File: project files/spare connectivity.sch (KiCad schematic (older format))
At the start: 1 part, among them J3 Target STDC-14

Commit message: some rerouting
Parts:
- added U3: STM32F103CBUx, Package_DFN_QFN:QFN-48-1EP_7x7mm_P0.5mm_EP5.6x5.6mm, symbol MCU_ST_STM32F1:STM32F103CBUx
- renumbered J3 to J6
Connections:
- net GNDD: now also U3.23 (VSS), U3.35 (VSS), U3.47 (VSS), U3.49 (VSS), U3.8 (VSSA)
- new net +3V3: U3.1 (VBAT), U3.24 (VDD), U3.36 (VDD), U3.48 (VDD), U3.9 (VDDA)
- new net AIN: U3.10 (PA0)
- new net BOOT_0: U3.44 (BOOT0)
- new net BOOT_1: U3.20 (PB2)
- new net Board_ID: U3.2 (PC13)
- new net OSC_IN: U3.5 (PD0)
- new net OSC_OUT: U3.6 (PD1)
- new net SELF_NRST: U3.7 (NRST)
- new net STLINK_LED: U3.30 (PA9)
- new net STLINK_RX: U3.13 (PA3)
- new net STLINK_TX: U3.12 (PA2)
- new net STLINK_USB_D+: U3.33 (PA12)
- new net STLINK_USB_D-: U3.32 (PA11)
- new net SWDCLK: U3.37 (PA14)
- new net SWDIO: U3.34 (PA13)
- new net SWO: U3.39 (PB3)
- new net T_JTDI: U3.17 (PA7)
- new net T_NRST_SWD: U3.18 (PB0)
- new net T_NRST_SWIM: U3.42 (PB6)
- new net T_NRST_SWIM_IN: U3.41 (PB5)
- new net T_SWDCLK: U3.15 (PA5), U3.26 (PB13)
- new net T_SWDIO: U3.27 (PB14)
- new net T_SWDIO_IN: U3.25 (PB12)
- new net T_SWIM: U3.22 (PB11), U3.45 (PB8)
- new net T_SWIM_IN: U3.21 (PB10), U3.43 (PB7), U3.46 (PB9)
- new net T_SWO: U3.31 (PA10)
- new net USB_RENUMn: U3.38 (PA15)
- no-connect marks 1 -> 10
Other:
- note added: "Second microcontroller is added for possibility to use different package.\nSolder one microcontroller only."
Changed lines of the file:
@@
 P 2950 3400
 AR Path="/5EC35CB1" Ref="#PWR?"  Part="1"
-AR Path="/5EC31CA9/5EC35CB1" Ref="#PWR0103"  Part="1"
-F 0 "#PWR0103" H 2950 3150 50  0001 C CNN
+AR Path="/5EC31CA9/5EC35CB1" Ref="#PWR050"  Part="1"
+F 0 "#PWR050" H 2950 3150 50  0001 C CNN
 F 1 "GNDD" H 2954 3245 50  0000 C CNN
 F 2 "" H 2950 3400 50  0001 C CNN
@@
 P 3200 3400
 AR Path="/5EC35CBA" Ref="#PWR?"  Part="1"
-AR Path="/5EC31CA9/5EC35CBA" Ref="#PWR0104"  Part="1"
-F 0 "#PWR0104" H 3200 3150 50  0001 C CNN
+AR Path="/5EC31CA9/5EC35CBA" Ref="#PWR051"  Part="1"
+F 0 "#PWR051" H 3200 3150 50  0001 C CNN
 F 1 "GNDD" H 3204 3245 50  0000 C CNN
 F 2 "" H 3200 3400 50  0001 C CNN
@@
 P 2950 2650
 AR Path="/5EC35CC7" Ref="J?"  Part="1"
-AR Path="/5EC31CA9/5EC35CC7" Ref="J3"  Part="1"
-F 0 "J3" H 2507 2696 50  0000 R CNN
+AR Path="/5EC31CA9/5EC35CC7" Ref="J6"  Part="1"
+F 0 "J6" H 2507 2696 50  0000 R CNN
 F 1 "Target STDC-14" H 2507 2605 50  0000 R CNN
 F 2 "Connector_PinHeader_1.27mm:PinHeader_2x07_P1.27mm_Vertical_SMD" H 2950 2650 50  0001 C CNN
@@
 Text GLabel 2900 1900 0    50   Input ~ 0
 T_Vref
+Wire Wire Line
+	9750 6100 9750 6050
+Wire Wire Line
+	9650 6050 9650 6100
+Connection ~ 9650 6100
+Wire Wire Line
+	9650 6100 9750 6100
+Wire Wire Line
+	9550 6050 9550 6100
+Connection ~ 9550 6100
+Wire Wire Line
+	9550 6100 9650 6100
+Wire Wire Line
+	9450 6050 9450 6100
+Connection ~ 9450 6100
+Wire Wire Line
+	9450 6100 9550 6100
+Wire Wire Line
+	9350 6050 9350 6100
+Wire Wire Line
+	9350 6100 9450 6100
+$Comp
+L power:GNDD #PWR053
+U 1 1 5EC6BDFB
+P 9750 6150
+F 0 "#PWR053" H 9750 5900 50  0001 C CNN
+F 1 "GNDD" H 9754 5995 50  0000 C CNN
+F 2 "" H 9750 6150 50  0001 C CNN
+F 3 "" H 9750 6150 50  0001 C CNN
+	1    9750 6150
+	1    0    0    -1
+$EndComp
+Wire Wire Line
+	9750 6150 9750 6100
+Connection ~ 9750 6100
+Text Notes 6700 6300 0    50   Italic 10
+Second microcontroller is added for possibility to use different package.\nSolder one microcontroller only.
+NoConn ~ 10150 5150
+NoConn ~ 10150 4950
+NoConn ~ 10150 4750
+NoConn ~ 10150 4450
+NoConn ~ 8850 5850
+NoConn ~ 8850 4750
+NoConn ~ 8850 4450
+NoConn ~ 8850 4150
+NoConn ~ 8850 4050
+Wire Wire Line
+	9350 3050 9350 3000
+Wire Wire Line
+	9450 3050 9450 3000
+Wire Wire Line
+	9550 3050 9550 3000
+Wire Wire Line
+	9650 3050 9650 3000
+Wire Wire Line
+	9750 3050 9750 3000
+$Comp
+L MCU_ST_STM32F1:STM32F103CBUx U3
+U 1 1 5EC6BE12
+P 9550 4550
+F 0 "U3" H 9850 3000 50  0000 C CNN
+F 1 "STM32F103CBUx" H 10100 3100 50  0000 C CNN
+F 2 "Package_DFN_QFN:QFN-48-1EP_7x7mm_P0.5mm_EP5.6x5.6mm" H 8950 3150 50  0001 R CNN
+F 3 "http://www.st.com/st-web-ui/static/active/en/resource/technical/document/datasheet/CD00161566.pdf" H 9550 4550 50  0001 C CNN
+	1    9550 4550
+	1    0    0    -1
+$EndComp
+Text GLabel 10150 5250 2    50   BiDi ~ 0
+STLINK_LED
+Text GLabel 8850 3650 0    50   Input ~ 0
+OSC_IN
+Text GLabel 8850 3750 0    50   Input ~ 0
+OSC_OUT
+Text GLabel 8850 3450 0    50   Input ~ 0
+BOOT_0
+Text GLabel 8850 3250 0    50   Input ~ 0
+SELF_NRST
+Text GLabel 8850 3950 0    50   Input ~ 0
+Board_ID
+Text GLabel 10150 4350 2    50   Input ~ 0
+AIN
+Text GLabel 10150 5450 2    50   Input ~ 0
+STLINK_USB_D-
+Text GLabel 10150 5550 2    50   Input ~ 0
+STLINK_USB_D+
+Text GLabel 10150 5350 2    50   Input ~ 0
+T_SWO
+Text GLabel 10150 5650 2    50   Input ~ 0
+SWDIO
+Text GLabel 10150 5750 2    50   Input ~ 0
+SWDCLK
+Text GLabel 10150 5850 2    50   Input ~ 0
+USB_RENUMn
+Text GLabel 8850 4650 0    50   Input ~ 0
+SWO
+Text GLabel 8850 4550 0    50   Input ~ 0
+BOOT_1
+Text GLabel 8850 5650 0    50   Input ~ 0
+T_SWDCLK
+Text GLabel 8850 4350 0    50   Input ~ 0
+T_NRST_SWD
+Text GLabel 8850 5350 0    50   Input ~ 0
+T_SWIM_IN
+Text GLabel 8850 5250 0    50   Input ~ 0
+T_SWIM_IN
+Text GLabel 8850 5050 0    50   Input ~ 0
+T_SWIM_IN
+Text GLabel 8850 4850 0    50   Input ~ 0
+T_NRST_SWIM_IN
+Text GLabel 8850 5750 0    50   Input ~ 0
+T_SWDIO
+Text GLabel 8850 4950 0    50   Input ~ 0
+T_NRST_SWIM
+Text GLabel 8850 5550 0    50   Input ~ 0
+T_SWDIO_IN
+Text GLabel 8850 5150 0    50   Input ~ 0
+T_SWIM
+Text GLabel 8850 5450 0    50   Input ~ 0
+T_SWIM
+Text GLabel 10150 4850 2    50   Input ~ 0
+T_SWDCLK
+Text GLabel 10150 4650 2    50   Output ~ 0
+STLINK_RX
+Text GLabel 10150 4550 2    50   Input ~ 0
+STLINK_TX
+Text GLabel 10150 5050 2    50   Input ~ 0
+T_JTDI
+Wire Wire Line
+	9350 3000 9450 3000
+Connection ~ 9450 3000
+Wire Wire Line
+	9450 3000 9550 3000
+Connection ~ 9550 3000
+Wire Wire Line
+	9550 3000 9650 3000
+Connection ~ 9650 3000
+Wire Wire Line
+	9650 3000 9750 3000
+$Comp
+L power:+3.3V #PWR052
+U 1 1 5EC6FD9F
+P 9550 3000
+F 0 "#PWR052" H 9550 2850 50  0001 C CNN
+F 1 "+3.3V" H 9565 3173 50  0000 C CNN
+F 2 "" H 9550 3000 50  0001 C CNN
+F 3 "" H 9550 3000 50  0001 C CNN
+	1    9550 3000
+	1    0    0    -1
+$EndComp
 $EndSCHEMATC

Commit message: fixes
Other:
- moved on the sheet: U3
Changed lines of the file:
@@
 Text Notes 2250 1800 0    50   ~ 0
 STDC-14: SAMTEC FTSH-107-01-L-DV-K-A
-Text GLabel 2800 3400 0    50   Output ~ 0
-GND_detect(h)
-Text GLabel 3350 3350 2    50   Output ~ 0
-GND_detect(h)
 $Comp
 L power:GNDD #PWR?
@@
 T_Vref
 Wire Wire Line
-	9750 6100 9750 6050
-Wire Wire Line
-	9650 6050 9650 6100
-Connection ~ 9650 6100
-Wire Wire Line
-	9650 6100 9750 6100
-Wire Wire Line
-	9550 6050 9550 6100
-Connection ~ 9550 6100
-Wire Wire Line
-	9550 6100 9650 6100
-Wire Wire Line
-	9450 6050 9450 6100
-Connection ~ 9450 6100
-Wire Wire Line
-	9450 6100 9550 6100
-Wire Wire Line
-	9350 6050 9350 6100
-Wire Wire Line
-	9350 6100 9450 6100
+	10050 4000 10050 3950
+Wire Wire Line
+	9950 3950 9950 4000
+Connection ~ 9950 4000
+Wire Wire Line
+	9950 4000 10050 4000
+Wire Wire Line
+	9850 3950 9850 4000
+Connection ~ 9850 4000
+Wire Wire Line
+	9850 4000 9950 4000
+Wire Wire Line
+	9750 3950 9750 4000
+Connection ~ 9750 4000
+Wire Wire Line
+	9750 4000 9850 4000
+Wire Wire Line
+	9650 3950 9650 4000
+Wire Wire Line
+	9650 4000 9750 4000
 $Comp
 L power:GNDD #PWR053
 U 1 1 5EC6BDFB
-P 9750 6150
-F 0 "#PWR053" H 9750 5900 50  0001 C CNN
-F 1 "GNDD" H 9754 5995 50  0000 C CNN
-F 2 "" H 9750 6150 50  0001 C CNN
-F 3 "" H 9750 6150 50  0001 C CNN
-	1    9750 6150
-	1    0    0    -1
-$EndComp
-Wire Wire Line
-	9750 6150 9750 6100
-Connection ~ 9750 6100
-Text Notes 6700 6300 0    50   Italic 10
+P 10050 4050
+F 0 "#PWR053" H 10050 3800 50  0001 C CNN
+F 1 "GNDD" H 10054 3895 50  0000 C CNN
+F 2 "" H 10050 4050 50  0001 C CNN
+F 3 "" H 10050 4050 50  0001 C CNN
+	1    10050 4050
+	1    0    0    -1
+$EndComp
+Wire Wire Line
+	10050 4050 10050 4000
+Connection ~ 10050 4000
+Text Notes 8350 4450 0    50   Italic 10
 Second microcontroller is added for possibility to use different package.\nSolder one microcontroller only.
-NoConn ~ 10150 5150
-NoConn ~ 10150 4950
-NoConn ~ 10150 4750
-NoConn ~ 10150 4450
-NoConn ~ 8850 5850
-NoConn ~ 8850 4750
-NoConn ~ 8850 4450
-NoConn ~ 8850 4150
-NoConn ~ 8850 4050
-Wire Wire Line
-	9350 3050 9350 3000
-Wire Wire Line
-	9450 3050 9450 3000
-Wire Wire Line
-	9550 3050 9550 3000
-Wire Wire Line
-	9650 3050 9650 3000
-Wire Wire Line
-	9750 3050 9750 3000
+NoConn ~ 10450 3050
+NoConn ~ 10450 2850
+NoConn ~ 10450 2650
+NoConn ~ 10450 2350
+NoConn ~ 9150 3750
+NoConn ~ 9150 2650
+NoConn ~ 9150 2350
+NoConn ~ 9150 2050
+NoConn ~ 9150 1950
+Wire Wire Line
+	9650 950  9650 900
+Wire Wire Line
+	9750 950  9750 900
+Wire Wire Line
+	9850 950  9850 900
+Wire Wire Line
+	9950 950  9950 900
+Wire Wire Line
+	10050 950  10050 900
 $Comp
 L MCU_ST_STM32F1:STM32F103CBUx U3
 U 1 1 5EC6BE12
-P 9550 4550
-F 0 "U3" H 9850 3000 50  0000 C CNN
-F 1 "STM32F103CBUx" H 10100 3100 50  0000 C CNN
-F 2 "Package_DFN_QFN:QFN-48-1EP_7x7mm_P0.5mm_EP5.6x5.6mm" H 8950 3150 50  0001 R CNN
-F 3 "http://www.st.com/st-web-ui/static/active/en/resource/technical/document/datasheet/CD00161566.pdf" H 9550 4550 50  0001 C CNN
-	1    9550 4550
-	1    0    0    -1
-$EndComp
-Text GLabel 10150 5250 2    50   BiDi ~ 0
+P 9850 2450
+F 0 "U3" H 10150 900 50  0000 C CNN
+F 1 "STM32F103CBUx" H 10400 1000 50  0000 C CNN
+F 2 "Package_DFN_QFN:QFN-48-1EP_7x7mm_P0.5mm_EP5.6x5.6mm" H 9250 1050 50  0001 R CNN
+F 3 "http://www.st.com/st-web-ui/static/active/en/resource/technical/document/datasheet/CD00161566.pdf" H 9850 2450 50  0001 C CNN
+	1    9850 2450
+	1    0    0    -1
+$EndComp
+Text GLabel 10450 3150 2    50   BiDi ~ 0
 STLINK_LED
-Text GLabel 8850 3650 0    50   Input ~ 0
+Text GLabel 9150 1550 0    50   Input ~ 0
 OSC_IN
-Text GLabel 8850 3750 0    50   Input ~ 0
+Text GLabel 9150 1650 0    50   Input ~ 0
 OSC_OUT
-Text GLabel 8850 3450 0    50   Input ~ 0
+Text GLabel 9150 1350 0    50   Input ~ 0
 BOOT_0
-Text GLabel 8850 3250 0    50   Input ~ 0
+Text GLabel 9150 1150 0    50   Input ~ 0
 SELF_NRST
-Text GLabel 8850 3950 0    50   Input ~ 0
+Text GLabel 9150 1850 0    50   Input ~ 0
 Board_ID
-Text GLabel 10150 4350 2    50   Input ~ 0
+Text GLabel 10450 2250 2    50   Input ~ 0
 AIN
-Text GLabel 10150 5450 2    50   Input ~ 0
+Text GLabel 10450 3350 2    50   Input ~ 0
 STLINK_USB_D-
-Text GLabel 10150 5550 2    50   Input ~ 0
+Text GLabel 10450 3450 2    50   Input ~ 0
 STLINK_USB_D+
-Text GLabel 10150 5350 2    50   Input ~ 0
+Text GLabel 10450 3250 2    50   Input ~ 0
 T_SWO
-Text GLabel 10150 5650 2    50   Input ~ 0
+Text GLabel 10450 3550 2    50   Input ~ 0
 SWDIO
-Text GLabel 10150 5750 2    50   Input ~ 0
+Text GLabel 10450 3650 2    50   Input ~ 0
 SWDCLK
-Text GLabel 10150 5850 2    50   Input ~ 0
+Text GLabel 10450 3750 2    50   Input ~ 0
 USB_RENUMn
-Text GLabel 8850 4650 0    50   Input ~ 0
+Text GLabel 9150 2550 0    50   Input ~ 0
 SWO
-Text GLabel 8850 4550 0    50   Input ~ 0
+Text GLabel 9150 2450 0    50   Input ~ 0
 BOOT_1
-Text GLabel 8850 5650 0    50   Input ~ 0
+Text GLabel 9150 3550 0    50   Input ~ 0
 T_SWDCLK
-Text GLabel 8850 4350 0    50   Input ~ 0
+Text GLabel 9150 2250 0    50   Input ~ 0
 T_NRST_SWD
-Text GLabel 8850 5350 0    50   Input ~ 0
+Text GLabel 9150 3250 0    50   Input ~ 0
 T_SWIM_IN
-Text GLabel 8850 5250 0    50   Input ~ 0
+Text GLabel 9150 3150 0    50   Input ~ 0
 T_SWIM_IN
-Text GLabel 8850 5050 0    50   Input ~ 0
+Text GLabel 9150 2950 0    50   Input ~ 0
 T_SWIM_IN
-Text GLabel 8850 4850 0    50   Input ~ 0
+Text GLabel 9150 2750 0    50   Input ~ 0
 T_NRST_SWIM_IN
-Text GLabel 8850 5750 0    50   Input ~ 0
+Text GLabel 9150 3650 0    50   Input ~ 0
 T_SWDIO
-Text GLabel 8850 4950 0    50   Input ~ 0
+Text GLabel 9150 2850 0    50   Input ~ 0
 T_NRST_SWIM
-Text GLabel 8850 5550 0    50   Input ~ 0
+Text GLabel 9150 3450 0    50   Input ~ 0
 T_SWDIO_IN
-Text GLabel 8850 5150 0    50   Input ~ 0
+Text GLabel 9150 3050 0    50   Input ~ 0
 T_SWIM
-Text GLabel 8850 5450 0    50   Input ~ 0
+Text GLabel 9150 3350 0    50   Input ~ 0
 T_SWIM
-Text GLabel 10150 4850 2    50   Input ~ 0
+Text GLabel 10450 2750 2    50   Input ~ 0
 T_SWDCLK
-Text GLabel 10150 4650 2    50   Output ~ 0
+Text GLabel 10450 2550 2    50   Output ~ 0
 STLINK_RX
-Text GLabel 10150 4550 2    50   Input ~ 0
+Text GLabel 10450 2450 2    50   Input ~ 0
 STLINK_TX
-Text GLabel 10150 5050 2    50   Input ~ 0
+Text GLabel 10450 2950 2    50   Input ~ 0
 T_JTDI
 Wire Wire Line
-	9350 3000 9450 3000
-Connection ~ 9450 3000
-Wire Wire Line
-	9450 3000 9550 3000
-Connection ~ 9550 3000
-Wire Wire Line
-	9550 3000 9650 3000
-Connection ~ 9650 3000
-Wire Wire Line
-	9650 3000 9750 3000
+	9650 900  9750 900
+Connection ~ 9750 900
+Wire Wire Line
+	9750 900  9850 900
+Connection ~ 9850 900
+Wire Wire Line
+	9850 900  9950 900
+Connection ~ 9950 900
+Wire Wire Line
+	9950 900  10050 900
 $Comp
 L power:+3.3V #PWR052
 U 1 1 5EC6FD9F
-P 9550 3000
-F 0 "#PWR052" H 9550 2850 50  0001 C CNN
-F 1 "+3.3V" H 9565 3173 50  0000 C CNN
-F 2 "" H 9550 3000 50  0001 C CNN
-F 3 "" H 9550 3000 50  0001 C CNN
-	1    9550 3000
-	1    0    0    -1
-$EndComp
+P 9850 900
+F 0 "#PWR052" H 9850 750 50  0001 C CNN
+F 1 "+3.3V" H 9865 1073 50  0000 C CNN
+F 2 "" H 9850 900 50  0001 C CNN
+F 3 "" H 9850 900 50  0001 C CNN
+	1    9850 900
+	1    0    0    -1
+$EndComp
+Text GLabel 3350 3350 2    50   Output ~ 0
+GND_detect(h)
+Text GLabel 2800 3400 0    50   Output ~ 0
+GND_detect(h)
 $EndSCHEMATC

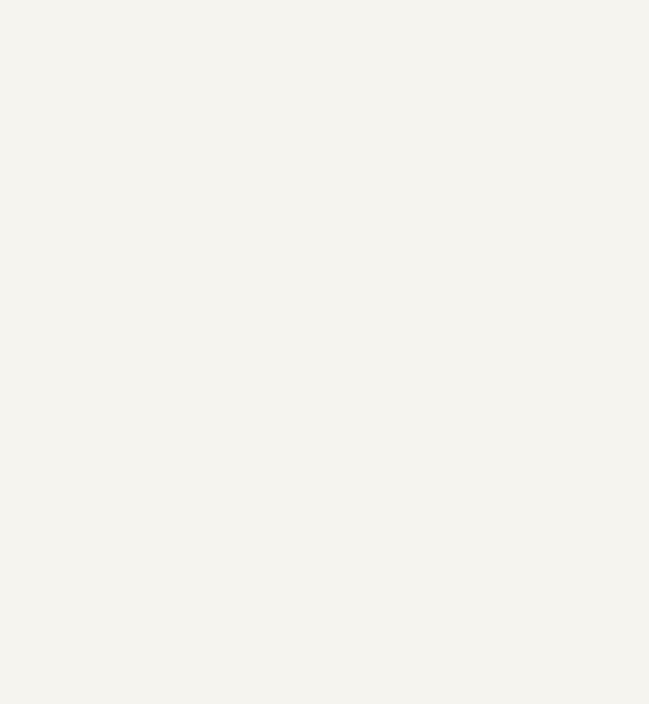
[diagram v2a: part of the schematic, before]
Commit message: updates with level converters
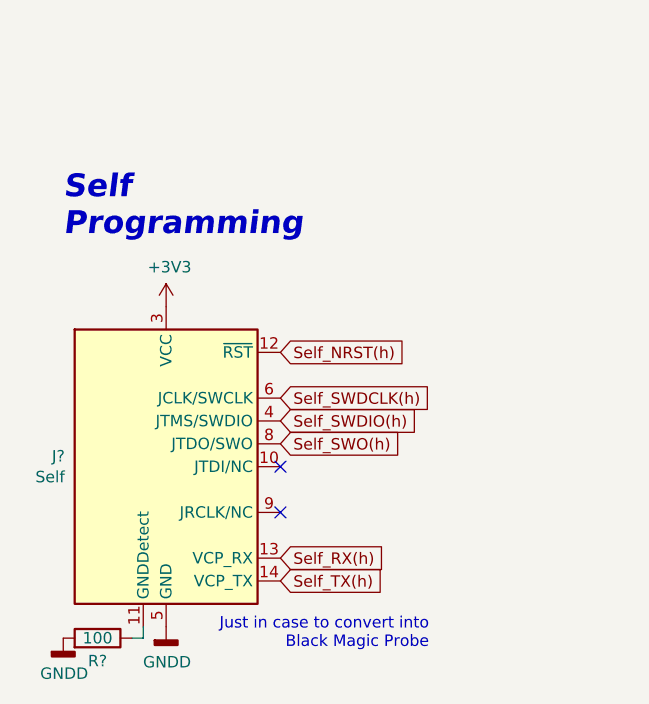
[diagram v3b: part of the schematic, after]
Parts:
- added J?: Self, Connector_PinHeader_1.27mm:PinHeader_2x07_P1.27mm_Vertical_SMD, symbol Connector:Conn_ST_STDC14
- added R?: 100, Resistor_SMD:R_0603_1608Metric, symbol Device:R
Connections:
- net +3V3: now also J?.3 (VCC)
- net GNDD: now also J?.5 (GND), J?.7 (GND), R?.2
- new net: J?.11 (GNDDetect), R?.1
- new net Self_NRST(h): J?.12 (~RST)
- new net Self_RX(h): J?.13 (VCP_RX)
- new net Self_SWDCLK(h): J?.6 (JCLK/SWCLK)
- new net Self_SWDIO(h): J?.4 (JTMS/SWDIO)
- new net Self_SWO(h): J?.8 (JTDO/SWO)
- new net Self_TX(h): J?.14 (VCP_TX)
- no-connect marks 10 -> 12
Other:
- note added: "Just in case to convert into\nBlack Magic Probe"
- note added: "Self\nProgramming"
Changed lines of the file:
@@
 Text GLabel 2800 3400 0    50   Output ~ 0
 GND_detect(h)
+Text Notes 2250 7550 2    50   ~ 0
+Just in case to convert into\nBlack Magic Probe
+Text GLabel 1600 7250 2    50   Input ~ 0
+Self_TX(h)
+Text GLabel 1600 7150 2    50   Input ~ 0
+Self_RX(h)
+$Comp
+L power:GNDD #PWR?
+U 1 1 5F1BD152
+P 1100 7450
+F 0 "#PWR?" H 1100 7200 50  0001 C CNN
+F 1 "GNDD" H 1104 7295 50  0000 C CNN
+F 2 "" H 1100 7450 50  0001 C CNN
+F 3 "" H 1100 7450 50  0001 C CNN
+	1    1100 7450
+	1    0    0    -1
+$EndComp
+Text GLabel 1600 6250 2    50   Input ~ 0
+Self_NRST(h)
+NoConn ~ 1600 6950
+Text GLabel 1600 6650 2    50   Input ~ 0
+Self_SWO(h)
+Text GLabel 1600 6450 2    50   Input ~ 0
+Self_SWDCLK(h)
+Text GLabel 1600 6550 2    50   Input ~ 0
+Self_SWDIO(h)
+$Comp
+L power:+3V3 #PWR?
+U 1 1 5F1BD15D
+P 1100 6050
+F 0 "#PWR?" H 1100 5900 50  0001 C CNN
+F 1 "+3V3" H 1115 6223 50  0000 C CNN
+F 2 "" H 1100 6050 50  0001 C CNN
+F 3 "" H 1100 6050 50  0001 C CNN
+	1    1100 6050
+	1    0    0    -1
+$EndComp
+NoConn ~ 1600 6750
+$Comp
+L Connector:Conn_ST_STDC14 J?
+U 1 1 5F1BD164
+P 1100 6750
+F 0 "J?" H 657 6796 50  0000 R CNN
+F 1 "Self" H 657 6705 50  0000 R CNN
+F 2 "Connector_PinHeader_1.27mm:PinHeader_2x07_P1.27mm_Vertical_SMD" H 1100 6750 50  0001 C CNN
+F 3 "https://www.st.com/content/ccc/resource/technical/document/user_manual/group1/99/49/91/b6/b2/3a/46/e5/DM00526767/files/DM00526767.pdf/jcr:content/translations/en.DM00526767.pdf" V 750 5500 50  0001 C CNN
+	1    1100 6750
+	1    0    0    -1
+$EndComp
+Text Notes 650  5750 0    100  Italic 20
+Self\nProgramming
+$Comp
+L Device:R R?
+U 1 1 5F1BD16B
+P 800 7500
+F 0 "R?" V 700 7500 50  0000 C CNN
+F 1 "100" V 800 7500 50  0000 C CNN
+F 2 "Resistor_SMD:R_0603_1608Metric" V 730 7500 50  0001 C CNN
+F 3 "~" H 800 7500 50  0001 C CNN
+	1    800  7500
+	0    1    -1   0
+$EndComp
+$Comp
+L power:GNDD #PWR?
+U 1 1 5F1BD171
+P 650 7500
+F 0 "#PWR?" H 650 7250 50  0001 C CNN
+F 1 "GNDD" H 654 7345 50  0000 C CNN
+F 2 "" H 650 7500 50  0001 C CNN
+F 3 "" H 650 7500 50  0001 C CNN
+	1    650  7500
+	1    0    0    -1
+$EndComp
+Wire Wire Line
+	950  7500 1000 7500
+Wire Wire Line
+	1000 7500 1000 7450
 $EndSCHEMATC
